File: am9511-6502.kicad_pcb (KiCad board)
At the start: 2 copper layers, 84.9 x 67.5 mm, 24 parts, among them J1 Conn_01x18_Pin, U1 AM9511A, U2 GAL16V8, U3 74HC112, U4 ADA-TPS61040, U5 74HC123, X1 4 MHz

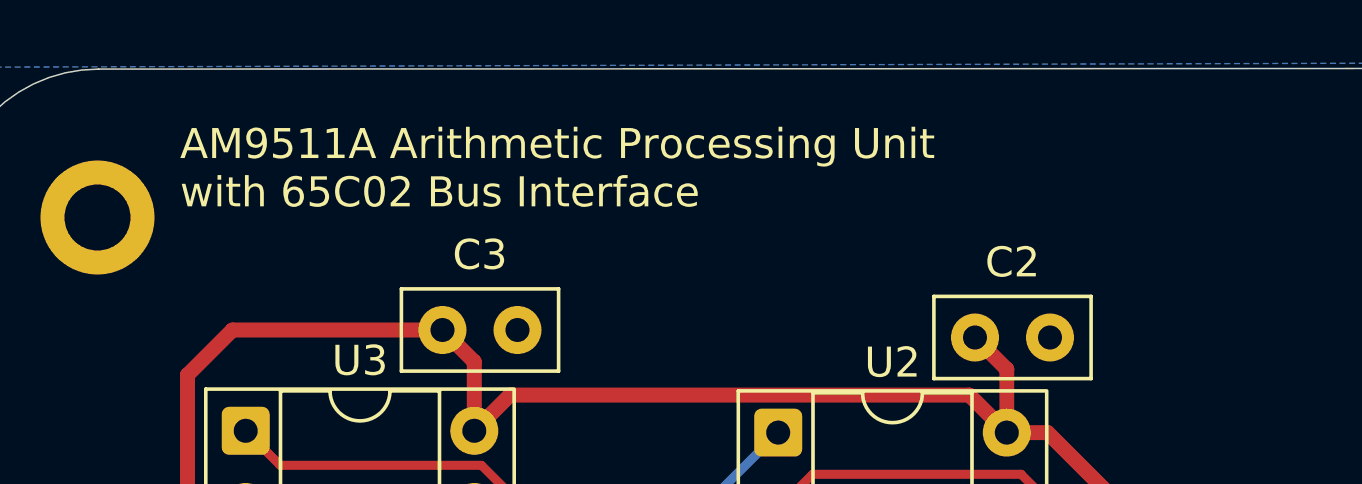
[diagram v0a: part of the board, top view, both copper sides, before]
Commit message: move custom symbols and footprints to project libraries
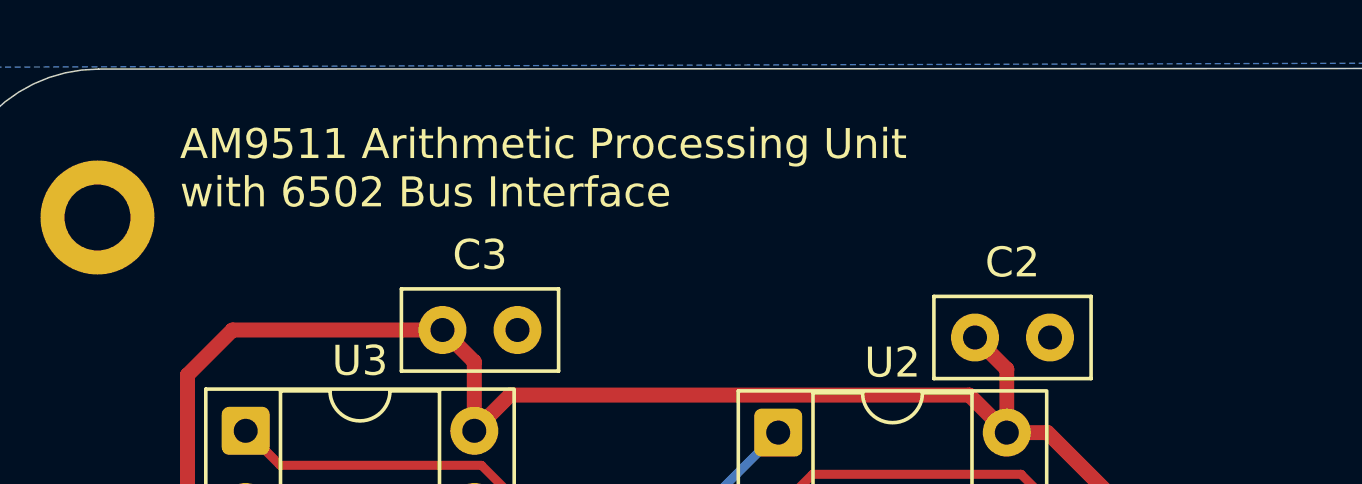
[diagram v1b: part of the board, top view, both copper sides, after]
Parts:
- U4: footprint Local:ADA-TPS61040 -> am9511-6502-footprints:ADA-TPS61040
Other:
- board text added: "AM9511 Arithmetic Processing Unit with 6502 Bus Interface"
- board text removed: "AM9511A Arithmetic Processing Unit with 65C02 Bus Interface"
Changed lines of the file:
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@@
 		)
 	)
-	(footprint "Local:ADA-TPS61040"
+	(footprint "am9511-6502-footprints:ADA-TPS61040"
 		(layer "F.Cu")
 		(at 154.093763 107 180)
@@
 		)
 		(property "Value" "ADA-TPS61040"
-			(at -6.737426 -0.067603 90)
-			(layer "F.Fab")
-			(effects
-				(font
-					(size 1 1)
-					(thickness 0.15)
-				)
-			)
-		)
-		(property "Datasheet" "https://www.adafruit.com/product/5644#technical-details"
+			(at -6.737426 -0.067603 270)
+			(layer "F.Fab")
+			(effects
+				(font
+					(size 1 1)
+					(thickness 0.15)
+				)
+			)
+		)
+		(property "Datasheet" ""
 			(at 0 0 180)
 			(unlocked yes)
@@
 			)
 		)
-		(property "Description" "Boost Converter"
+		(property "Description" ""
 			(at 0 0 180)
 			(unlocked yes)
@@
 		)
 	)
-	(gr_text "AM9511A Arithmetic Processing Unit \nwith 65C02 Bus Interface"
+	(gr_text "AM9511 Arithmetic Processing Unit \nwith 6502 Bus Interface"
 		(at 110.25 54.75 0)
 		(layer "F.SilkS")
